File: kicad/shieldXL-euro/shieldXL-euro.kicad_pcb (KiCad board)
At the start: 2 copper layers, 98 x 108 mm, 148 parts, among them J101 Eurorack power, J102 IN L, J103 IN R, J104 OUT L, J105 OUT R, J106 MIDI IN, J107 MIDI OUT, J108 DX07S024WJ1R350, J109 USB 1, J110 USB 2, J111 USB 3, J112 Pi USB, inner stack, J113 Pi USB, outer stack, J115 CORONE I/1, J116 CORONE I/2, J117 CORONE O/1, J118 CORONE O/2, J119 CORONE O/3, J120 CORONE O/4, J121 Corone, J122 ii, Q1 ASFL1-12.288MHZ-LCS-T, SW1 D6R00 F1 LFS, SW2 D6R00 F1 LFS, SW3 D6R00 F1 LFS, U1 CS4270, U101 TL074, U102 USBLC6-2SC6, U103 USBLC6-2SC6, U104 USBLC6-2SC6, U105 74LVC1G125, U11 TPS793475DBVR, U2 HCPL-0631-500E, X1 RASPI_BOARD_B+#_E3

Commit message: Copper-to-edge clearance 0.025 -> 0.3 mm; pours refilled
shieldXL's 0.025 mm let the pours run to the board's edge; 0.3 mm is a
fab's usual minimum. The 14 stitching vias on the grid's outer row (0.25 mm
in) are removed; the rest of the stitching still joins the pours.

Co-Authored-By: Claude Opus 5.5 <noreply@anthropic.com>
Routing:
- net GND: vias 102 -> 88
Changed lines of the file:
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@@
-	)
-	(via
-		(at 199.1 42.7)
-		(size 0.6)
-		(drill 0.3)
-		(layers "F.Cu" "B.Cu")
-		(net "GND")
 	)
 	(via
@@
 	)
 	(via
-		(at 199.1 52.7)
-		(size 0.6)
-		(drill 0.3)
-		(layers "F.Cu" "B.Cu")
-		(net "GND")
-	)
-	(via
 		(at 164.1 122.7)
 		(size 0.6)
@@
 	)
 	(via
-		(at 199.1 47.7)
-		(size 0.6)
-		(drill 0.3)
-		(layers "F.Cu" "B.Cu")
-		(net "GND")
-	)
-	(via
 		(at 112.578558 48.15)
 		(size 0.6)
@@
 	)
 	(via
-		(at 194.1 147.7)
-		(size 0.6)
-		(drill 0.3)
-		(layers "F.Cu" "B.Cu")
-		(net "GND")
-	)
-	(via
 		(at 189.1 82.7)
 		(size 0.6)
@@
 	)
 	(via
-		(at 199.1 77.7)
-		(size 0.6)
-		(drill 0.3)
-		(layers "F.Cu" "B.Cu")
-		(net "GND")
-	)
-	(via
 		(at 124.1 97.7)
 		(size 0.6)
@@
 	)
 	(via
-		(at 199.1 87.7)
-		(size 0.6)
-		(drill 0.3)
-		(layers "F.Cu" "B.Cu")
-		(net "GND")
-	)
-	(via
 		(at 109.1 77.7)
 		(size 0.6)
@@
 	)
 	(via
-		(at 199.1 62.7)
-		(size 0.6)
-		(drill 0.3)
-		(layers "F.Cu" "B.Cu")
-		(net "GND")
-	)
-	(via
-		(at 199.1 97.7)
-		(size 0.6)
-		(drill 0.3)
-		(layers "F.Cu" "B.Cu")
-		(net "GND")
-	)
-	(via
 		(at 126.6 72.3)
 		(size 0.6)
@@
 	)
 	(via
-		(at 199.1 67.7)
-		(size 0.6)
-		(drill 0.3)
-		(layers "F.Cu" "B.Cu")
-		(net "GND")
-	)
-	(via
 		(at 104.1 52.7)
 		(size 0.6)
@@
 	)
 	(via
-		(at 199.1 82.7)
-		(size 0.6)
-		(drill 0.3)
-		(layers "F.Cu" "B.Cu")
-		(net "GND")
-	)
-	(via
 		(at 154.1 62.7)
 		(size 0.6)
@@
 	)
 	(via
-		(at 199.1 57.7)
-		(size 0.6)
-		(drill 0.3)
-		(layers "F.Cu" "B.Cu")
-		(net "GND")
-	)
-	(via
-		(at 199.1 72.7)
-		(size 0.6)
-		(drill 0.3)
-		(layers "F.Cu" "B.Cu")
-		(net "GND")
-	)
-	(via
 		(at 142.2 57.2)
 		(size 0.6)
@@
 		(layers "F.Cu" "B.Cu")
 		(free yes)
-		(net "GND")
-	)
-	(via
-		(at 119.1 147.7)
-		(size 0.6)
-		(drill 0.3)
-		(layers "F.Cu" "B.Cu")
-		(net "GND")
-	)
-	(via
-		(at 199.1 92.7)
-		(size 0.6)
-		(drill 0.3)
-		(layers "F.Cu" "B.Cu")
 		(net "GND")
 	)
@@
 	)
 	(segment
-		(start 168.2 147.25)
-		(end 168 147.05)
-		(width 0.8)
-		(layer "F.Cu")
-		(net "/eurorack/USB3_VBUS")
-	)
-	(segment
 		(start 155.75 147.05)
 		(end 167.9 147.05)
@@
 	)
 	(segment
+		(start 193.4 143.55)
+		(end 190.4 146.55)
+		(width 0.8)
+		(layer "F.Cu")
+		(net "/eurorack/USB3_VBUS")
+	)
+	(segment
 		(start 168 146.95)
 		(end 168 146.85)
@@
 	)
 	(segment
+		(start 190.4 146.55)
+		(end 168.3 146.55)
+		(width 0.8)
+		(layer "F.Cu")
+		(net "/eurorack/USB3_VBUS")
+	)
+	(segment
 		(start 193.4 141.76)
 		(end 193.4 143.55)
@@
 	)
 	(segment
-		(start 168 147.05)
+		(start 168.3 146.55)
 		(end 168 146.85)
 		(width 0.8)
@@
 		(width 0.8)
 		(layer "F.Cu")
-		(net "/eurorack/USB3_VBUS")
-	)
-	(segment
-		(start 193.4 143.55)
-		(end 189.7 147.25)
-		(width 0.8)
-		(layer "F.Cu")
-		(net "/eurorack/USB3_VBUS")
-	)
-	(segment
-		(start 189.7 147.25)
-		(end 168.2 147.25)
-		(width 0.8)
-		(layer "F.Cu")

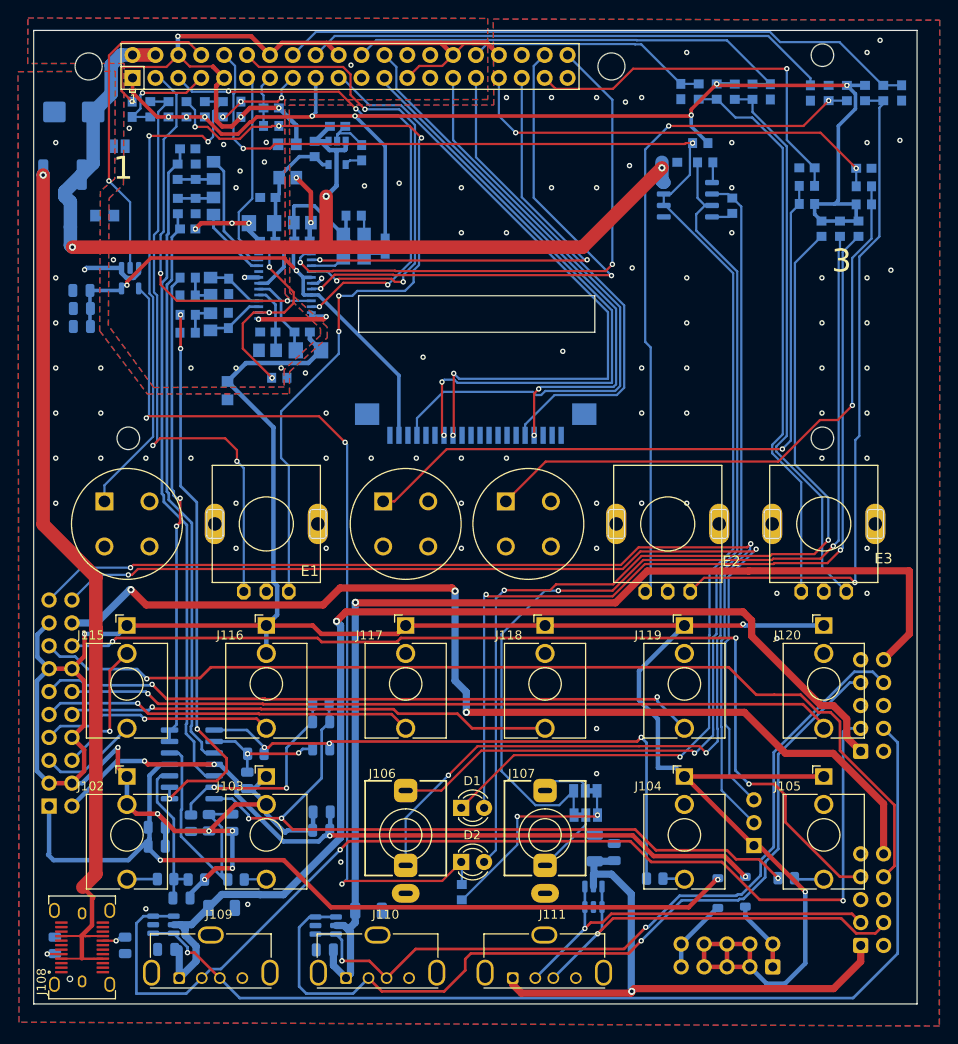
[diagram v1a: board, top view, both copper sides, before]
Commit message: Board: tracks pulled in from the top edge and display holes
Co-Authored-By: Claude Opus 5.5 <noreply@anthropic.com>
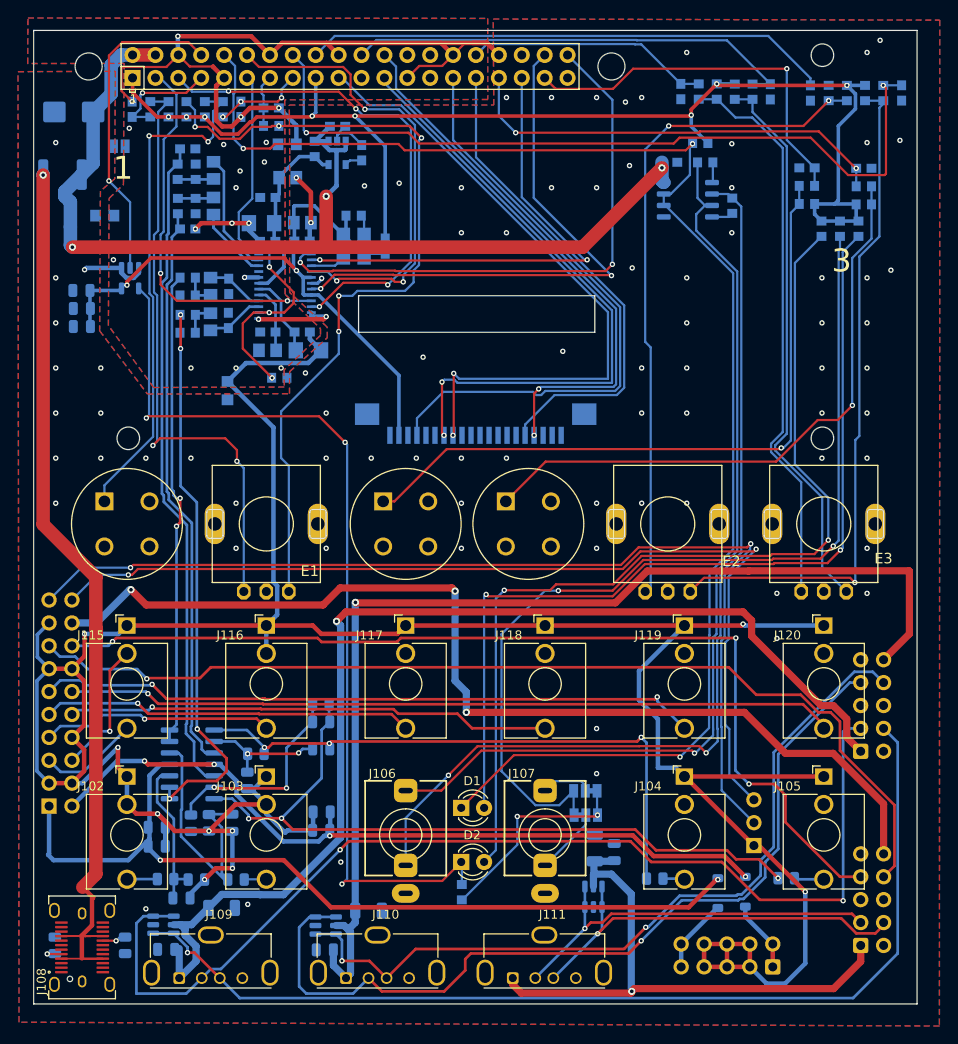
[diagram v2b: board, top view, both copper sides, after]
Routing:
- net B2: track 71.0 -> 88.0 mm, vias 0 -> 2
- net AGND: track 340.5 -> 338.7 mm, vias 24 -> 23
- net GND: track 126.8 -> 125.8 mm
- net /eurorack/OUTL_AMP: track 65.2 -> 64.6 mm

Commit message: Board: routed and DRC clean
0 unconnected, schematic parity clean, every track 0.3 mm from the edge.
Left in DRC: the pours at 0.297 mm (fill arc tolerance), J108's pad A12 by
its own locating peg (stock footprint), the encoders' lug cut-outs, three
courtyard overlaps (J101/D101, J101/D102, J108/J102) and silkscreen overlaps.

Co-Authored-By: Claude Opus 5.5 <noreply@anthropic.com>
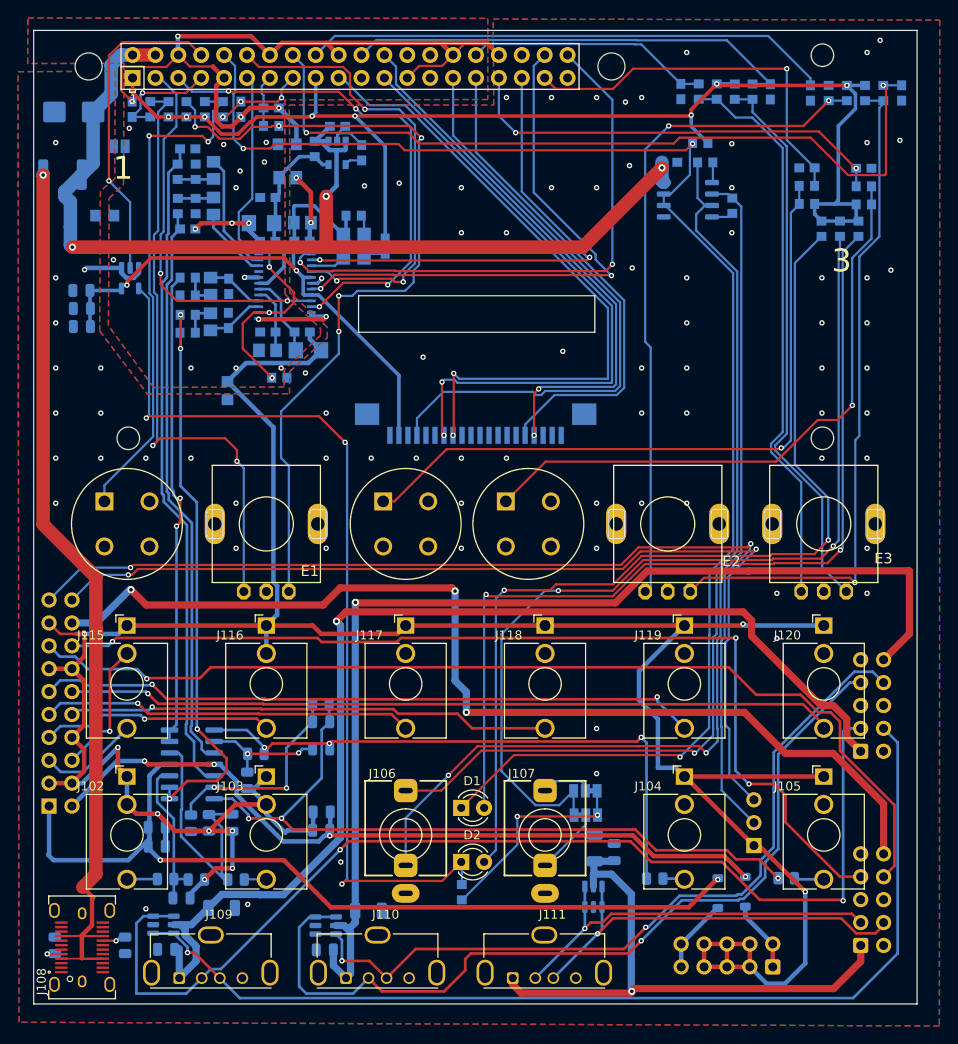
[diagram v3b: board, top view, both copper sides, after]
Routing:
- net AGND: track 338.7 -> 323.2 mm

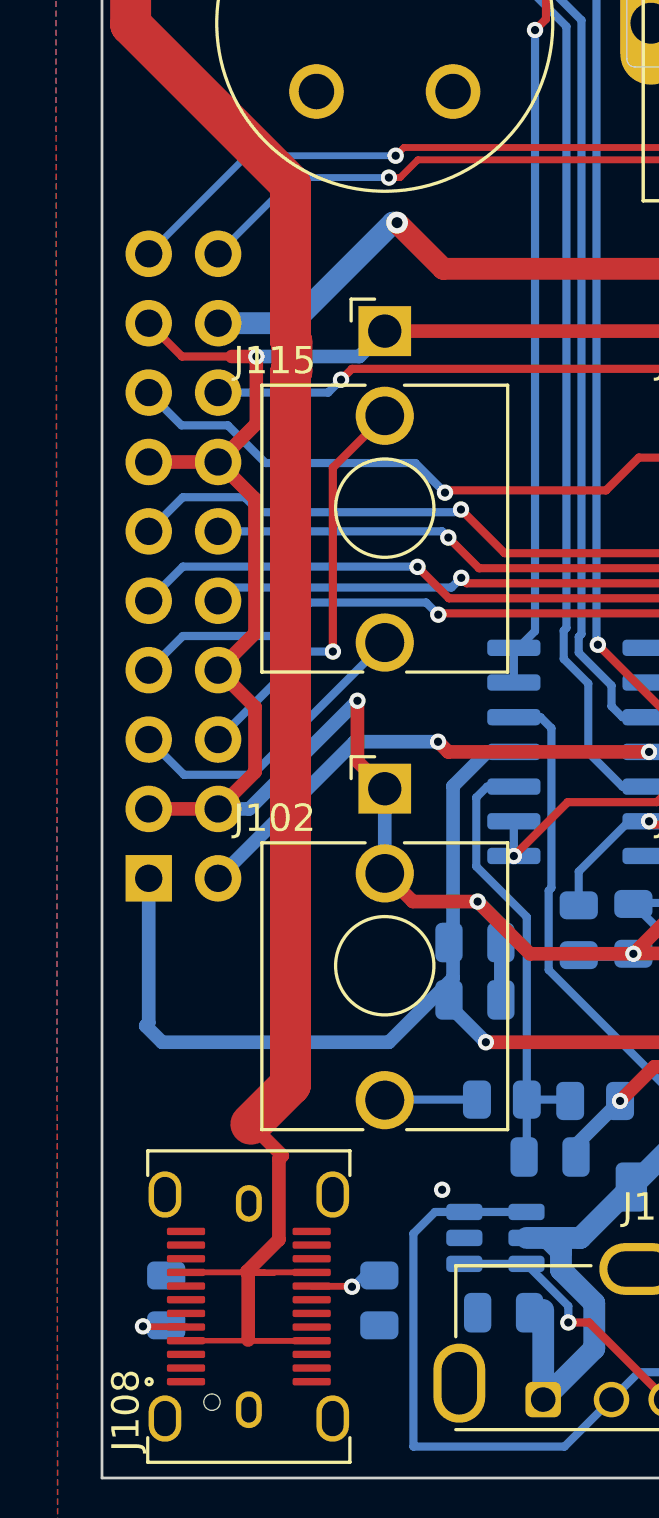
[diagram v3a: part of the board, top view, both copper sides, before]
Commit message: J122 (ii) labelled on the back: GND / SCL / SDA, a bar beside GND
ii headers have no fixed order between modules (monome's i2c guide: connect
by name, find GND by its mark), so each pin is named and GND is marked.

Co-Authored-By: Claude Opus 5.5 <noreply@anthropic.com>
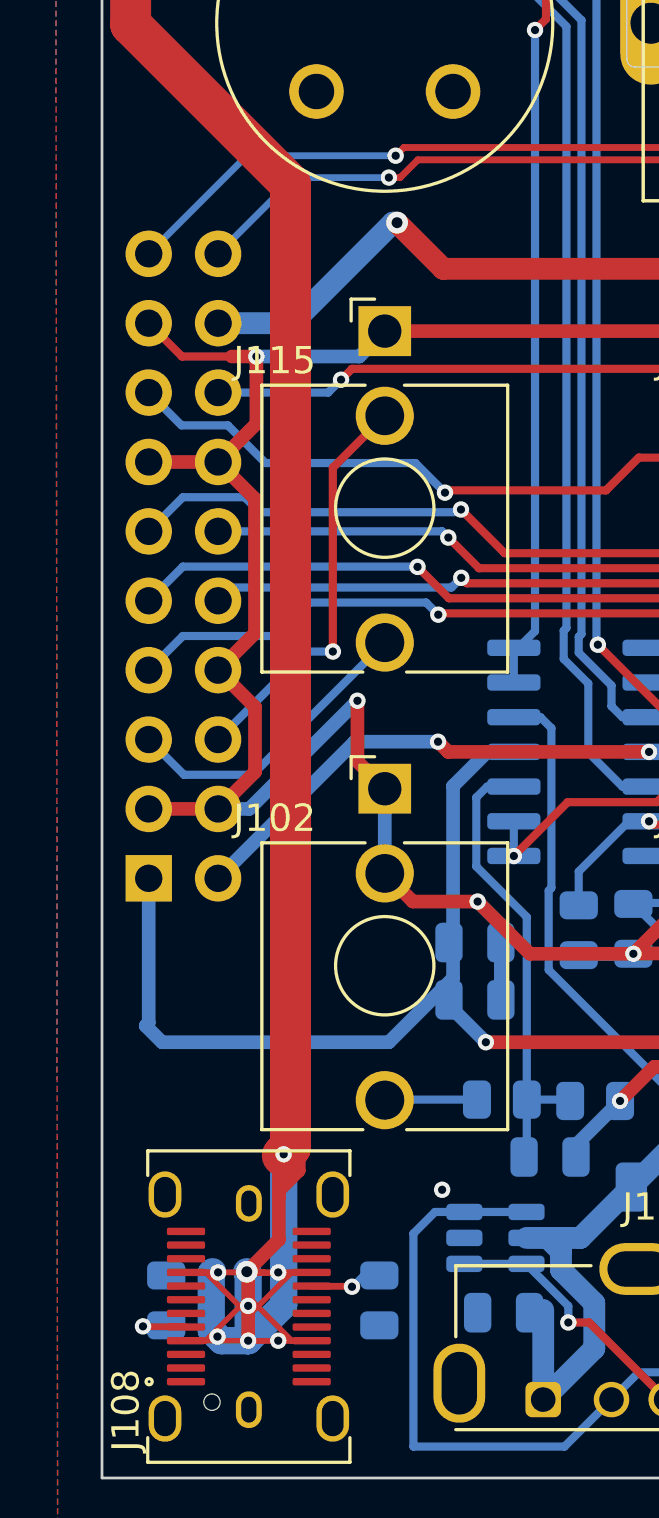
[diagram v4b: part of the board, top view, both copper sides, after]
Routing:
- net /eurorack/VBUS_C: track 108.4 -> 138.6 mm, vias 1 -> 9
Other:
- board text added: "GND"
- board text added: "SCL"
- board text added: "SDA"
